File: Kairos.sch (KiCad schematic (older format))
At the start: 45 parts, among them Q1 NSS40301MZ4T1G, SW1 SW_RST1, U1 ATMEGA32U2-AU, Y1 Crystal_GND24

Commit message: Add in the RGBs to PCB (Not organized yet)
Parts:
- CR1, CR10, CR11, CR12, CR13, CR14, CR2, CR3, CR4, CR5, CR6, CR7, CR8, CR9: footprint (none) -> Capacitors_SMD:C_0603
- LED13, LED14: footprint (none) -> WS2812B:WS2812B
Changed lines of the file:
@@
 F 0 "CR1" H 6375 5500 50  0000 L CNN
 F 1 "100nF" H 6375 5300 50  0000 L CNN
-F 2 "" H 6388 5250 50  0001 C CNN
+F 2 "Capacitors_SMD:C_0603" H 6388 5250 50  0001 C CNN
 F 3 "" H 6350 5400 50  0001 C CNN
 	1    6350 5400
@@
 F 0 "CR2" H 6675 5500 50  0000 L CNN
 F 1 "100nF" H 6675 5300 50  0000 L CNN
-F 2 "" H 6688 5250 50  0001 C CNN
+F 2 "Capacitors_SMD:C_0603" H 6688 5250 50  0001 C CNN
 F 3 "" H 6650 5400 50  0001 C CNN
 	1    6650 5400
@@
 F 0 "CR3" H 6975 5500 50  0000 L CNN
 F 1 "100nF" H 6975 5300 50  0000 L CNN
-F 2 "" H 6988 5250 50  0001 C CNN
+F 2 "Capacitors_SMD:C_0603" H 6988 5250 50  0001 C CNN
 F 3 "" H 6950 5400 50  0001 C CNN
 	1    6950 5400
@@
 F 0 "CR4" H 7275 5500 50  0000 L CNN
 F 1 "100nF" H 7275 5300 50  0000 L CNN
-F 2 "" H 7288 5250 50  0001 C CNN
+F 2 "Capacitors_SMD:C_0603" H 7288 5250 50  0001 C CNN
 F 3 "" H 7250 5400 50  0001 C CNN
 	1    7250 5400
@@
 F 0 "CR5" H 7575 5500 50  0000 L CNN
 F 1 "100nF" H 7575 5300 50  0000 L CNN
-F 2 "" H 7588 5250 50  0001 C CNN
+F 2 "Capacitors_SMD:C_0603" H 7588 5250 50  0001 C CNN
 F 3 "" H 7550 5400 50  0001 C CNN
 	1    7550 5400
@@
 F 0 "CR6" H 7875 5500 50  0000 L CNN
 F 1 "100nF" H 7875 5300 50  0000 L CNN
-F 2 "" H 7888 5250 50  0001 C CNN
+F 2 "Capacitors_SMD:C_0603" H 7888 5250 50  0001 C CNN
 F 3 "" H 7850 5400 50  0001 C CNN
 	1    7850 5400
@@
 F 0 "CR7" H 6375 6000 50  0000 L CNN
 F 1 "100nF" H 6375 5800 50  0000 L CNN
-F 2 "" H 6388 5750 50  0001 C CNN
+F 2 "Capacitors_SMD:C_0603" H 6388 5750 50  0001 C CNN
 F 3 "" H 6350 5900 50  0001 C CNN
 	1    6350 5900
@@
 F 0 "CR8" H 6675 6000 50  0000 L CNN
 F 1 "100nF" H 6675 5800 50  0000 L CNN
-F 2 "" H 6688 5750 50  0001 C CNN
+F 2 "Capacitors_SMD:C_0603" H 6688 5750 50  0001 C CNN
 F 3 "" H 6650 5900 50  0001 C CNN
 	1    6650 5900
@@
 F 0 "CR9" H 6975 6000 50  0000 L CNN
 F 1 "100nF" H 6975 5800 50  0000 L CNN
-F 2 "" H 6988 5750 50  0001 C CNN
+F 2 "Capacitors_SMD:C_0603" H 6988 5750 50  0001 C CNN
 F 3 "" H 6950 5900 50  0001 C CNN
 	1    6950 5900
@@
 F 0 "CR10" H 7275 6000 50  0000 L CNN
 F 1 "100nF" H 7275 5800 50  0000 L CNN
-F 2 "" H 7288 5750 50  0001 C CNN
+F 2 "Capacitors_SMD:C_0603" H 7288 5750 50  0001 C CNN
 F 3 "" H 7250 5900 50  0001 C CNN
 	1    7250 5900
@@
 F 0 "CR11" H 7575 6000 50  0000 L CNN
 F 1 "100nF" H 7575 5800 50  0000 L CNN
-F 2 "" H 7588 5750 50  0001 C CNN
+F 2 "Capacitors_SMD:C_0603" H 7588 5750 50  0001 C CNN
 F 3 "" H 7550 5900 50  0001 C CNN
 	1    7550 5900
@@
 F 0 "CR12" H 7875 6000 50  0000 L CNN
 F 1 "100nF" H 7875 5800 50  0000 L CNN
-F 2 "" H 7888 5750 50  0001 C CNN
+F 2 "Capacitors_SMD:C_0603" H 7888 5750 50  0001 C CNN
 F 3 "" H 7850 5900 50  0001 C CNN
 	1    7850 5900
@@
 F 0 "LED13" H 11100 6650 60  0000 C CNN
 F 1 "WS2812B" H 11100 7450 60  0000 C CNN
-F 2 "" V 11050 7050 60  0000 C CNN
+F 2 "WS2812B:WS2812B" V 11050 7050 60  0001 C CNN
 F 3 "" V 11050 7050 60  0000 C CNN
 	1    11100 7050
@@
 F 0 "LED14" H 11100 7625 60  0000 C CNN
 F 1 "WS2812B" H 11100 8425 60  0000 C CNN
-F 2 "" V 11050 8025 60  0000 C CNN
+F 2 "WS2812B:WS2812B" V 11050 8025 60  0001 C CNN
 F 3 "" V 11050 8025 60  0000 C CNN
 	1    11100 8025
@@
 F 0 "CR13" H 8175 6000 50  0000 L CNN
 F 1 "100nF" H 8175 5800 50  0000 L CNN
-F 2 "" H 8188 5750 50  0001 C CNN
+F 2 "Capacitors_SMD:C_0603" H 8188 5750 50  0001 C CNN
 F 3 "" H 8150 5900 50  0001 C CNN
 	1    8150 5900
@@
 F 0 "CR14" H 8475 6000 50  0000 L CNN
 F 1 "100nF" H 8475 5800 50  0000 L CNN
-F 2 "" H 8488 5750 50  0001 C CNN
+F 2 "Capacitors_SMD:C_0603" H 8488 5750 50  0001 C CNN
 F 3 "" H 8450 5900 50  0001 C CNN
 	1    8450 5900

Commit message: Some progress in wiring
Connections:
- net RGBLED: now also U1.9 ((TXD1/INT3)PD3); no longer U1.20 ((PCINT6)PB6)
- net COL0: now reaches U1.26 ((PCINT10)PC4)
- net COL1: now reaches U1.5 ((PCINT11/AIN2)PC2)
- net COL2: now reaches U1.6 ((OC.0B/INT0)PD0)
- net ROW0: now reaches U1.7 ((AIN0/INT1)PD1)
- net ROW1: now reaches U1.8 ((RXD1/AIN1/INT2)PD2)
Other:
- moved on the sheet: R5
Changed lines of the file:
@@
 Text GLabel 9750 1750 0    60   Input ~ 0
-RGBLED
-Text GLabel 4350 2550 2    60   Input ~ 0
 RGBLED
 Text GLabel 800  3450 0    60   Input ~ 0
@@
 L R R5
 U 1 1 59512333
-P 4250 1700
-F 0 "R5" V 4330 1700 50  0000 C CNN
-F 1 "1.5k" V 4250 1700 50  0000 C CNN
-F 2 "Resistors_SMD:R_0603" V 4180 1700 50  0001 C CNN
-F 3 "" H 4250 1700 50  0001 C CNN
-	1    4250 1700
-	1    0    0    -1
+P 4450 1200
+F 0 "R5" V 4530 1200 50  0000 C CNN
+F 1 "1.5k" V 4450 1200 50  0000 C CNN
+F 2 "Resistors_SMD:R_0603" V 4380 1200 50  0001 C CNN
+F 3 "" H 4450 1200 50  0001 C CNN
+	1    4450 1200
+	0    -1   -1   0
 $EndComp
 $Comp
@@
 Connection ~ 850  2700
 Wire Wire Line
-	4150 2650 4250 2650
-Wire Wire Line
-	4250 1200 4150 1200
+	4150 2650 5100 2650
+Wire Wire Line
+	4150 1200 4300 1200
 Wire Wire Line
 	3850 1000 3850 900
@@
 	10150 1750 9750 1750
 Wire Wire Line
-	4150 2550 4350 2550
-Wire Wire Line
 	6200 5750 8450 5750
 Wire Wire Line
@@
 Wire Wire Line
 	1300 2150 1250 2150
-Wire Wire Line
-	4250 1200 4250 1550
-Wire Wire Line
-	4250 2650 4250 1850
 Wire Wire Line
 	1250 2550 1950 2550
@@
 Connection ~ 6650 5250
 Connection ~ 6350 5250
+Text GLabel 4150 3750 2    60   Input ~ 0
+COL1
+Text GLabel 4150 3850 2    60   Input ~ 0
+COL0
+Text GLabel 4150 2850 2    60   Input ~ 0
+COL2
+Text GLabel 4150 2950 2    60   Input ~ 0
+ROW0
+Text GLabel 4150 3050 2    60   Input ~ 0
+ROW1
+Text GLabel 4150 3150 2    60   Input ~ 0
+RGBLED
+Wire Wire Line
+	5100 2650 5100 1200
+Wire Wire Line
+	5100 1200 4600 1200
 $EndSCHEMATC

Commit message: Mark pinout
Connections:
- net ROW2: now reaches U1.10 ((INT5/AIN3)PD4)
- net ROW3: now reaches U1.11 ((XCK/AIN4/PCINT12)PD5)
- net COL7: now reaches U1.12 ((~RTS~/AIN5/INT6)PD6)
- net COL6: now reaches U1.14 ((~SS~/PCINT0)PB0)
- net COL5: now reaches U1.15 ((SCLK/PCINT1)PB1)
- net COL4: now reaches U1.16 ((PDI/MOSI/PCINT2)PB2)
- net COL3: now reaches U1.17 ((PD0/MISO/PCINT3)PB3)
- net ROW4: now reaches U1.18 ((T1/PCINT4)PB4)
- net ROW5: now reaches U1.19 ((PCINT5)PB5)
- net ROW6: now reaches U1.20 ((PCINT6)PB6)
- net ROW7: now reaches U1.22 ((INT4/ICP1/CLK0)PC7)
- net ROW8: now reaches U1.23 ((OC.1A/PCINT8)PC6)
- net ROW9: now reaches U1.25 ((PCINT9/OC.1B)PC5)
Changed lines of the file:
@@
 Wire Wire Line
 	5100 1200 4600 1200
+Text GLabel 4150 3250 2    60   Input ~ 0
+ROW2
+Text GLabel 4150 3350 2    60   Input ~ 0
+ROW3
+Text GLabel 4150 3950 2    60   Input ~ 0
+ROW9
+Text GLabel 4150 4050 2    60   Input ~ 0
+ROW8
+Text GLabel 4150 4150 2    60   Input ~ 0
+ROW7
+Text GLabel 4150 2550 2    60   Input ~ 0
+ROW6
+Text GLabel 4150 2450 2    60   Input ~ 0
+ROW5
+Text GLabel 4150 2350 2    60   Input ~ 0
+ROW4
+Text GLabel 4150 2250 2    60   Input ~ 0
+COL3
+Text GLabel 4150 2150 2    60   Input ~ 0
+COL4
+Text GLabel 4150 2050 2    60   Input ~ 0
+COL5
+Text GLabel 4150 1950 2    60   Input ~ 0
+COL6
+Text GLabel 4150 3450 2    60   Input ~ 0
+COL7
 $EndSCHEMATC

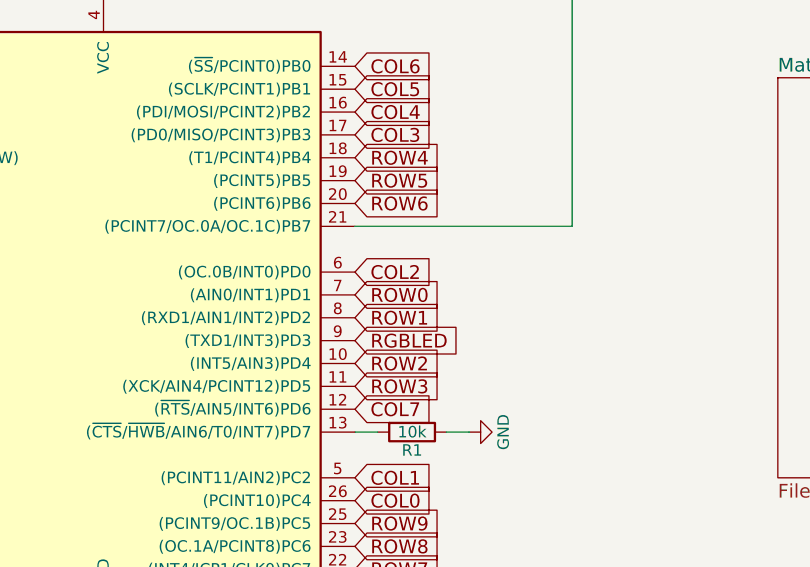
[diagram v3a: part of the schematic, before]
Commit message: Placed diodes in preliminary positions
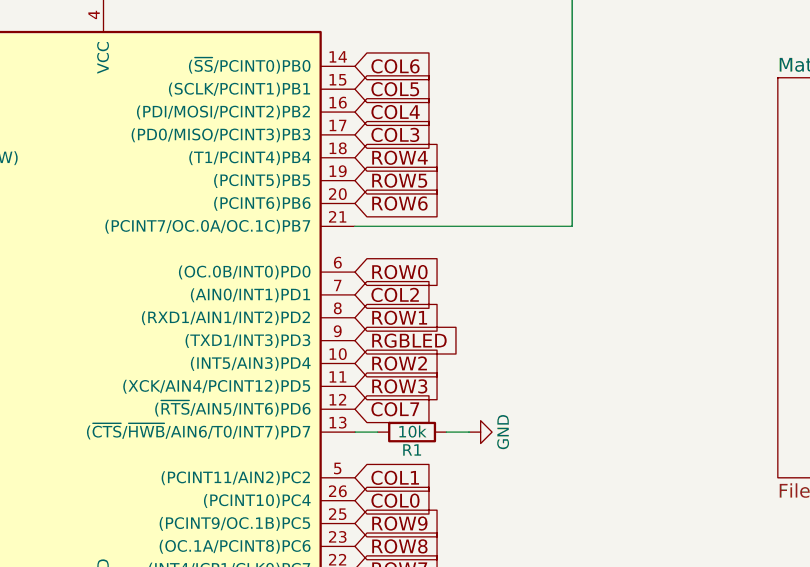
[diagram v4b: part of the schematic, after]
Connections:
- net COL2: now also U1.7 ((AIN0/INT1)PD1); no longer U1.6 ((OC.0B/INT0)PD0)
- net ROW0: now also U1.6 ((OC.0B/INT0)PD0); no longer U1.7 ((AIN0/INT1)PD1)
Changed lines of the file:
@@
 Text GLabel 4150 3850 2    60   Input ~ 0
 COL0
+Text GLabel 4150 2950 2    60   Input ~ 0
+COL2
 Text GLabel 4150 2850 2    60   Input ~ 0
-COL2
-Text GLabel 4150 2950 2    60   Input ~ 0
 ROW0
 Text GLabel 4150 3050 2    60   Input ~ 0
